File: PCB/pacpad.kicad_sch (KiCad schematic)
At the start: 9 parts, among them SW1 SW_Push, SW2 SW_Push, SW3 SW_Push, SW4 SW_Push, SW5 RotaryEncoder_Switch, U1 MOUDLE-SEEEDUINO-XIAO, U2 ER_OLEDM0.91_1x-I2C

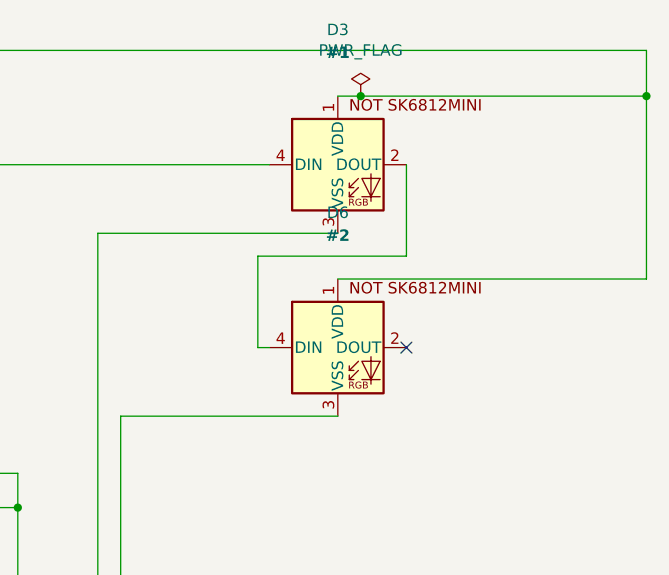
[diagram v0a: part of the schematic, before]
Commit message: Added everything except the firmkware
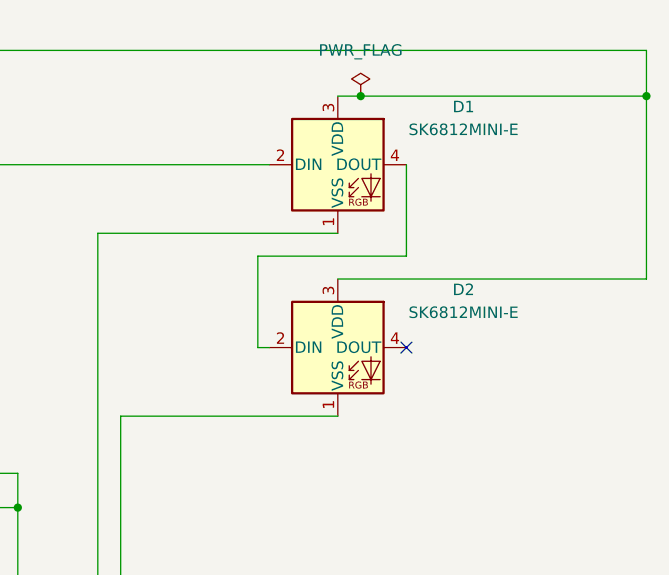
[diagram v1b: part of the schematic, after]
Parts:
- removed D3: #1, pacpadig:SK6812MINI-E_fixed, symbol pacpad:SK6812MINI-E
- removed D6: #2, pacpadig:SK6812MINI-E_fixed, symbol pacpad:SK6812MINI-E
- added D1, D2: SK6812MINI-E, pacpad_F:SK6812MINI-E_fixed, symbol LED:SK6812MINI-E
- U1: footprint pacpadig:XIAO-Generic-Hybrid-14P-2.54-21X17.8MM -> pacpad_F:XIAO-Generic-Hybrid-14P-2.54-21X17.8MM
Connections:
- net GND: now also D1.1 (VSS), D2.1 (VSS)
- net at U1.14 (5V): now also D1.3 (VDD), D2.3 (VDD)
- net at U1.4 (PA11_A3_D3): now also D1.2 (DIN)
- new net: D1.4 (DOUT), D2.2 (DIN)
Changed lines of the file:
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@@
-	)
-	(symbol
-		(lib_id "pacpad:SK6812MINI-E")
-		(at 218.44 48.26 0)
-		(unit 1)
-		(body_style 1)
-		(exclude_from_sim no)
-		(in_bom yes)
-		(on_board yes)
-		(in_pos_files yes)
-		(dnp no)
-		(property "Reference" "D6"
-			(at 218.44 33.2739 0)
-			(show_name no)
-			(do_not_autoplace no)
-			(effects
-				(font
-					(size 1.27 1.27)
-				)
-			)
-		)
-		(property "Value" "#2"
-			(at 218.44 35.814 0)
-			(show_name no)
-			(do_not_autoplace no)
-			(effects
-				(font
-					(size 1.27 1.27)
-					(thickness 0.254)
-					(bold yes)
-				)
-			)
-		)
-		(property "Footprint" "pacpadig:SK6812MINI-E_fixed"
-			(at 219.71 55.88 0)
-			(hide yes)
-			(show_name no)
-			(do_not_autoplace no)
-			(effects
-				(font
-					(size 1.27 1.27)
-				)
-				(justify left top)
-			)
-		)
-		(property "Datasheet" "https://cdn-shop.adafruit.com/product-files/4960/4960_SK6812MINI-E_REV02_EN.pdf"
-			(at 220.98 57.785 0)
-			(hide yes)
-			(show_name no)
-			(do_not_autoplace no)
-			(effects
-				(font
-					(size 1.27 1.27)
-				)
-				(justify left top)
-			)
-		)
-		(property "Description" "RGB LED with integrated controller"
-			(at 218.44 48.26 0)
-			(hide yes)
-			(show_name no)
-			(do_not_autoplace no)
-			(effects
-				(font
-					(size 1.27 1.27)
-				)
-			)
-		)
-		(pin "4"
-		)
-		(pin "2"
-		)
-		(pin "3"
-		)
-		(pin "1"
-		)
-		(instances
-			(project "pacpad"
-				(path "/f4a3dc9d-3954-4143-987a-129041dc4ed1"
-					(reference "D6")
-					(unit 1)
-				)
-			)
-		)
 	)
 	(symbol
@@
 	)
 	(symbol
-		(lib_id "pacpad:SK6812MINI-E")
-		(at 218.44 27.94 0)
-		(unit 1)
-		(body_style 1)
-		(exclude_from_sim no)
-		(in_bom yes)
-		(on_board yes)
-		(in_pos_files yes)
-		(dnp no)
-		(property "Reference" "D3"
-			(at 218.44 12.9539 0)
-			(show_name no)
-			(do_not_autoplace no)
-			(effects
-				(font
-					(size 1.27 1.27)
-				)
-			)
-		)
-		(property "Value" "#1"
-			(at 218.44 15.494 0)
-			(show_name no)
-			(do_not_autoplace no)
-			(effects
-				(font
-					(size 1.27 1.27)
-					(thickness 0.254)
-					(bold yes)
-				)
-			)
-		)
-		(property "Footprint" "pacpadig:SK6812MINI-E_fixed"
-			(at 219.71 35.56 0)
-			(hide yes)
-			(show_name no)
-			(do_not_autoplace no)
-			(effects
-				(font
-					(size 1.27 1.27)
-				)
-				(justify left top)
-			)
-		)
-		(property "Datasheet" "https://cdn-shop.adafruit.com/product-files/4960/4960_SK6812MINI-E_REV02_EN.pdf"
-			(at 220.98 37.465 0)
-			(hide yes)
-			(show_name no)
-			(do_not_autoplace no)
-			(effects
-				(font
-					(size 1.27 1.27)
-				)
-				(justify left top)
-			)
-		)
-		(property "Description" "RGB LED with integrated controller"
-			(at 218.44 27.94 0)
-			(hide yes)
-			(show_name no)
-			(do_not_autoplace no)
-			(effects
-				(font
-					(size 1.27 1.27)
-				)
-			)
-		)
-		(pin "4"
-		)
-		(pin "2"
-		)
-		(pin "3"
-		)
-		(pin "1"
-		)
-		(instances
-			(project "pacpad"
-				(path "/f4a3dc9d-3954-4143-987a-129041dc4ed1"
-					(reference "D3")
-					(unit 1)
-				)
-			)
-		)
-	)
-	(symbol
 		(lib_id "Switch:SW_Push")
 		(at 172.72 78.74 0)
@@
 	)
 	(symbol
+		(lib_id "LED:SK6812MINI-E")
+		(at 218.44 27.94 0)
+		(unit 1)
+		(body_style 1)
+		(exclude_from_sim no)
+		(in_bom yes)
+		(on_board yes)
+		(in_pos_files yes)
+		(dnp no)
+		(fields_autoplaced yes)
+		(property "Reference" "D1"
+			(at 232.41 21.5198 0)
+			(show_name no)
+			(do_not_autoplace no)
+			(effects
+				(font
+					(size 1.27 1.27)
+				)
+			)
+		)
+		(property "Value" "SK6812MINI-E"
+			(at 232.41 24.0598 0)
+			(show_name no)
+			(do_not_autoplace no)
+			(effects
+				(font
+					(size 1.27 1.27)
+				)
+			)
+		)
+		(property "Footprint" "pacpad_F:SK6812MINI-E_fixed"
+			(at 219.71 35.56 0)
+			(hide yes)
+			(show_name no)
+			(do_not_autoplace no)
+			(effects
+				(font
+					(size 1.27 1.27)
+				)
+				(justify left top)
+			)
+		)
+		(property "Datasheet" "https://www.lcsc.com/datasheet/C5149201.pdf"
+			(at 220.98 37.465 0)
+			(hide yes)
+			(show_name no)
+			(do_not_autoplace no)
+			(effects
+				(font
+					(size 1.27 1.27)
+				)
+				(justify left top)
+			)
+		)
+		(property "Description" "RGB LED with integrated controller"
+			(at 218.44 27.94 0)
+			(hide yes)
+			(show_name no)
+			(do_not_autoplace no)
+			(effects
+				(font
+					(size 1.27 1.27)
+				)
+			)
+		)
+		(pin "3"
+		)
+		(pin "2"
+		)
+		(pin "4"
+		)
+		(pin "1"
+		)
+		(instances
+			(project "pacpad"
+				(path "/f4a3dc9d-3954-4143-987a-129041dc4ed1"
+					(reference "D1")
+					(unit 1)
+				)
+			)
+		)
+	)
+	(symbol
 		(lib_id "Switch:SW_Push")
 		(at 171.45 66.04 0)
@@
 	)
 	(symbol
+		(lib_id "LED:SK6812MINI-E")
+		(at 218.44 48.26 0)
+		(unit 1)
+		(body_style 1)
+		(exclude_from_sim no)
+		(in_bom yes)
+		(on_board yes)
+		(in_pos_files yes)
+		(dnp no)
+		(fields_autoplaced yes)
+		(property "Reference" "D2"
+			(at 232.41 41.8398 0)
+			(show_name no)
+			(do_not_autoplace no)
+			(effects
+				(font
+					(size 1.27 1.27)
+				)
+			)
+		)
+		(property "Value" "SK6812MINI-E"
+			(at 232.41 44.3798 0)
+			(show_name no)
+			(do_not_autoplace no)
+			(effects
+				(font
+					(size 1.27 1.27)
+				)
+			)
+		)
+		(property "Footprint" "pacpad_F:SK6812MINI-E_fixed"
+			(at 219.71 55.88 0)
+			(hide yes)
+			(show_name no)
+			(do_not_autoplace no)
+			(effects
+				(font
+					(size 1.27 1.27)
+				)
+				(justify left top)
+			)
+		)
+		(property "Datasheet" "https://www.lcsc.com/datasheet/C5149201.pdf"
+			(at 220.98 57.785 0)
+			(hide yes)
+			(show_name no)
+			(do_not_autoplace no)
+			(effects
+				(font
+					(size 1.27 1.27)
+				)
+				(justify left top)
+			)
+		)
+		(property "Description" "RGB LED with integrated controller"
+			(at 218.44 48.26 0)
+			(hide yes)
+			(show_name no)
+			(do_not_autoplace no)
+			(effects
+				(font
+					(size 1.27 1.27)
+				)
+			)
+		)
+		(pin "3"
+		)
+		(pin "2"
+		)
+		(pin "4"
+		)
+		(pin "1"
+		)
+		(instances
+			(project "pacpad"
+				(path "/f4a3dc9d-3954-4143-987a-129041dc4ed1"
+					(reference "D2")
+					(unit 1)
+				)
+			)
+		)
+	)
+	(symbol
 		(lib_id "XIAO_RP2040:MOUDLE-SEEEDUINO-XIAO")
 		(at 134.62 85.09 0)
@@
 			)
 		)
-		(property "Footprint" "pacpadig:XIAO-Generic-Hybrid-14P-2.54-21X17.8MM"
+		(property "Footprint" "pacpad_F:XIAO-Generic-Hybrid-14P-2.54-21X17.8MM"
 			(at 118.11 82.55 0)
 			(hide yes)
